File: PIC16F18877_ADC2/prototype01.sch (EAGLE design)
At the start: 16 parts, among them CN1 PIC_CN_H, CN2 ADC_IN, SW1 10-XX, U1 PIC16F18877-I/P, U2 AE-AQM1602A

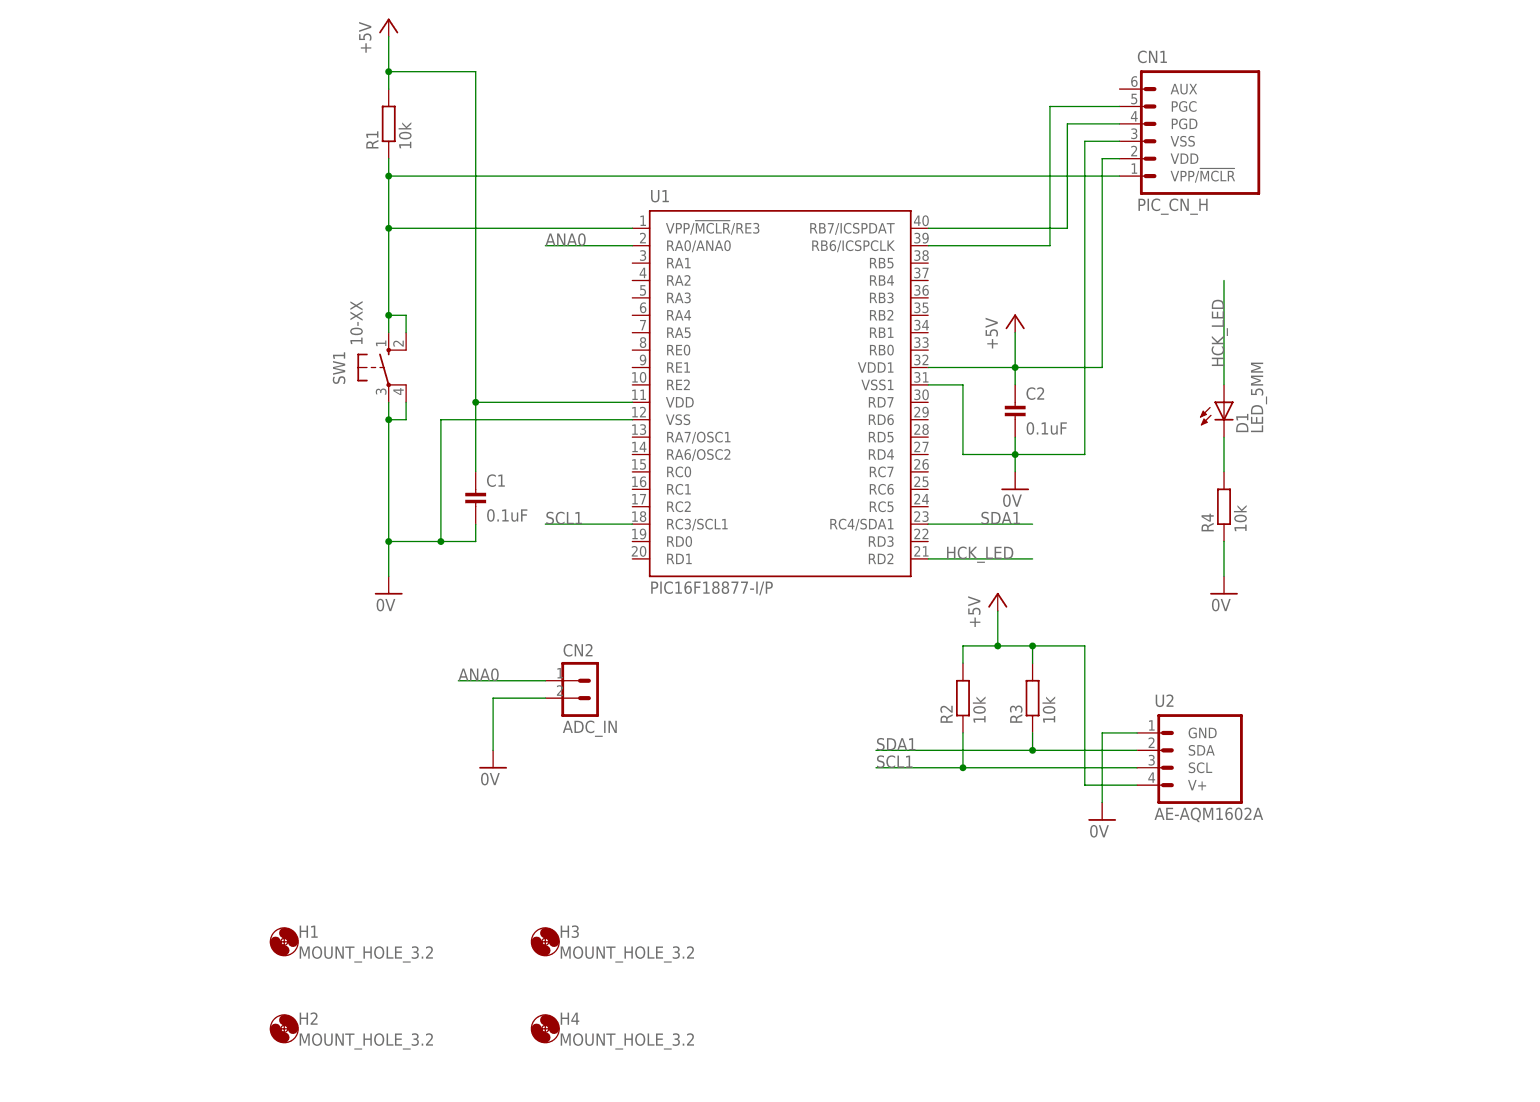
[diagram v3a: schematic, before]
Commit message: microSDカード接続のための回路図／コードを追加
sdcard、sdcard_testは、動作確認用の一時的なファイルなので後日必ず削除してください。
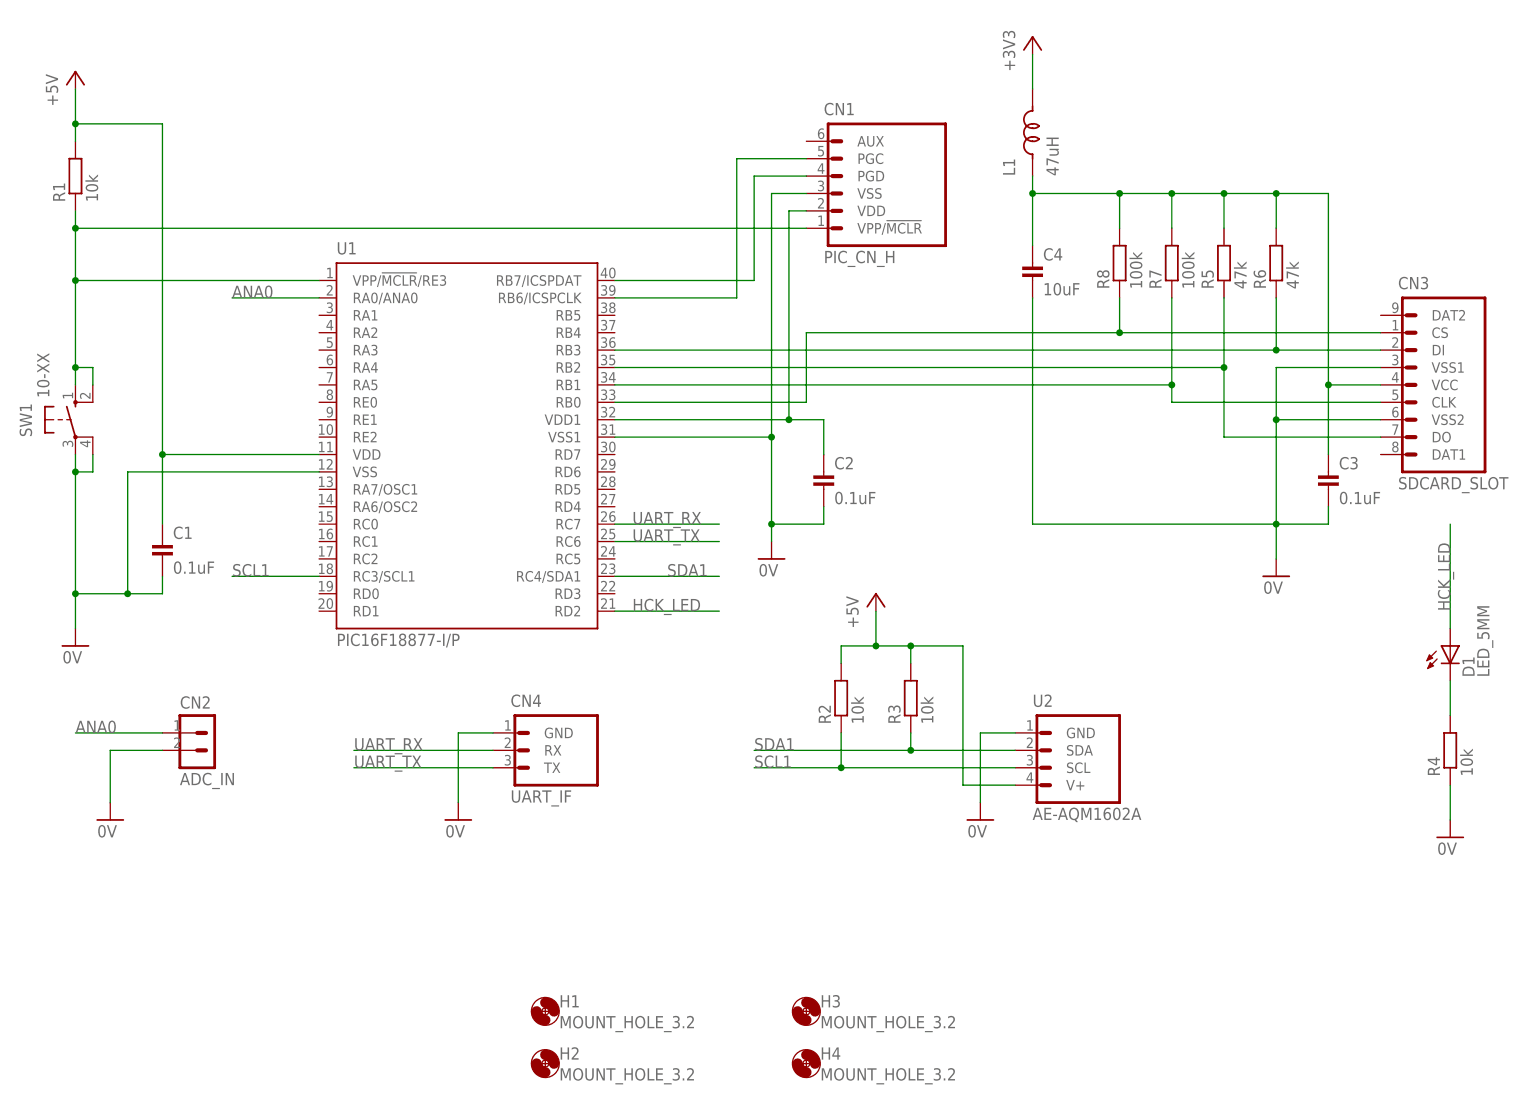
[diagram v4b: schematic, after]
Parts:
- added C3: 0.1uF, Parts:CAP_200MIL
- added C4: 10uF, Parts:CAP_200MIL
- added CN3: SDCARD_SLOT, PartsForProto:SDCARD_SLOT
- added CN4: UART_IF, PartsForProto:UART_IF
- added L1: 47uH, Parts:TC5026-22UH-060
- added R5, R6: 47k, Parts:RESISTOR_300MIL
- added R7, R8: 100k, Parts:RESISTOR_300MIL
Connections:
- new net +3V3: L1.2
- new net N$10: C2.1, CN1.VDD, U1.VDD1
- new net N$12: CN3.DI, R6.1, U1.RB3
- new net N$6: CN3.CLK, R7.1, U1.RB1
- new net N$7: CN3.CS, R8.1, U1.RB0
- new net N$8: CN3.DO, R5.1, U1.RB2
- new net N$9: C3.1, C4.1, CN3.VCC, L1.1, R5.2, R6.2, R7.2, R8.2
- new net UART_RX: CN4.RX, U1.RC7
- new net UART_TX: CN4.TX, U1.RC6
- net +5V: no longer C2.1, CN1.VDD, U1.VDD1
- net 0V: now also C3.2, C4.2, CN3.VSS1, CN3.VSS2, CN4.GND
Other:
- moved on the sheet: C1, C2, CN1, CN2, D1, H1, H2, H3, H4, R1, R2, R3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

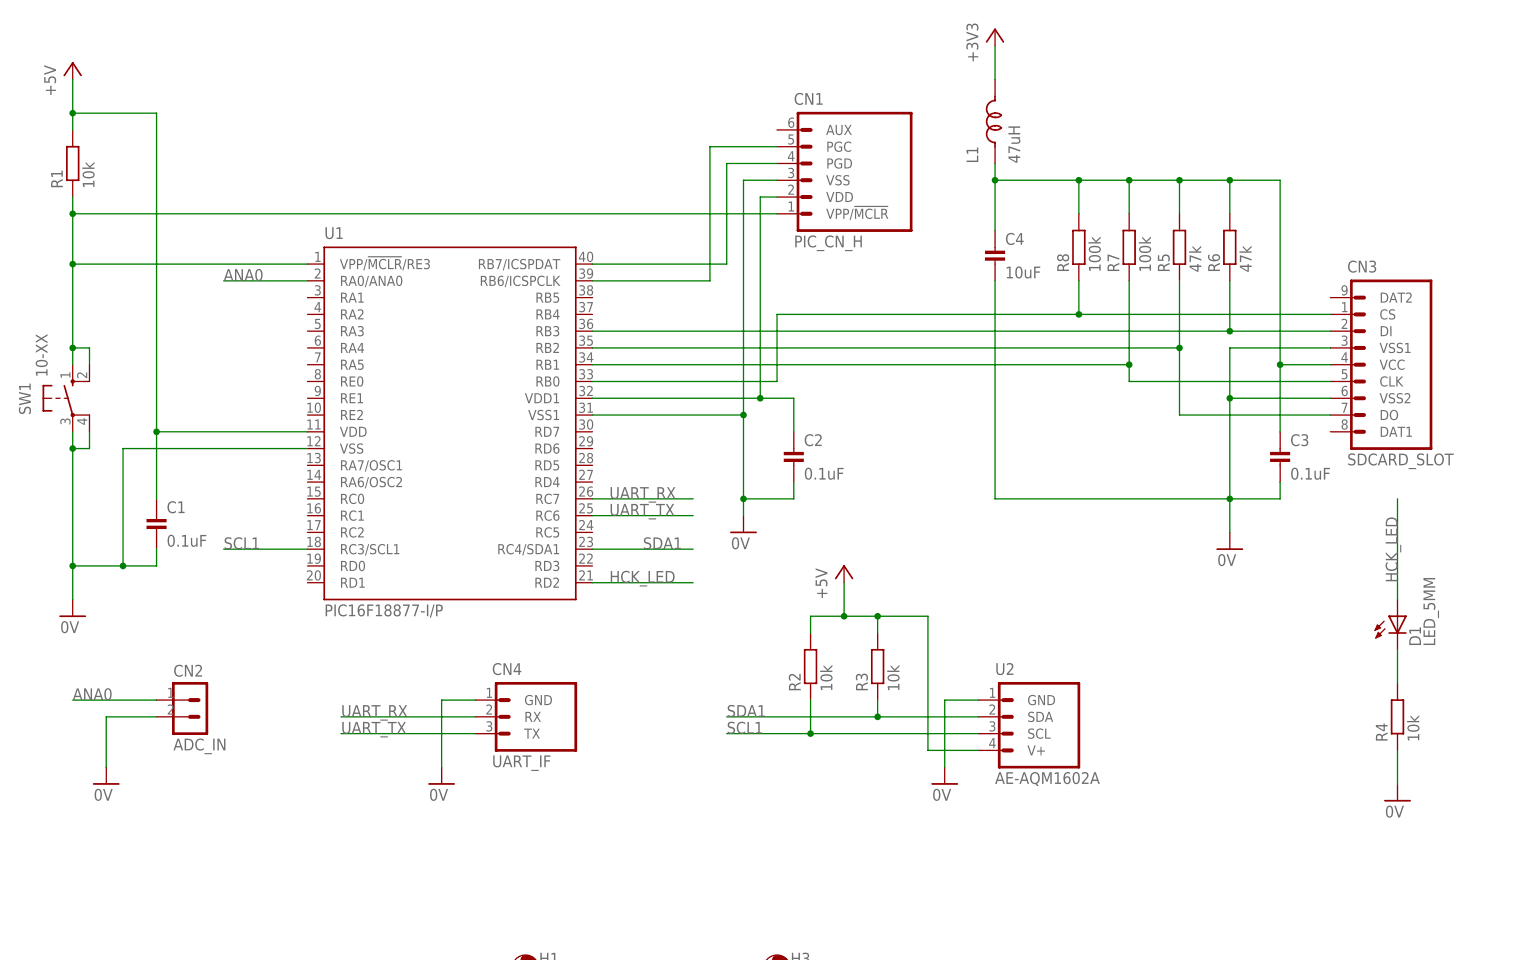
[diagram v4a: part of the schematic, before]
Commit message: 回路図を修正
マイクロＳＤカードスロットＤＩＰ化キットの使用を前提とするよう修正
http://akizukidenshi.com/catalog/g/gK-05488/
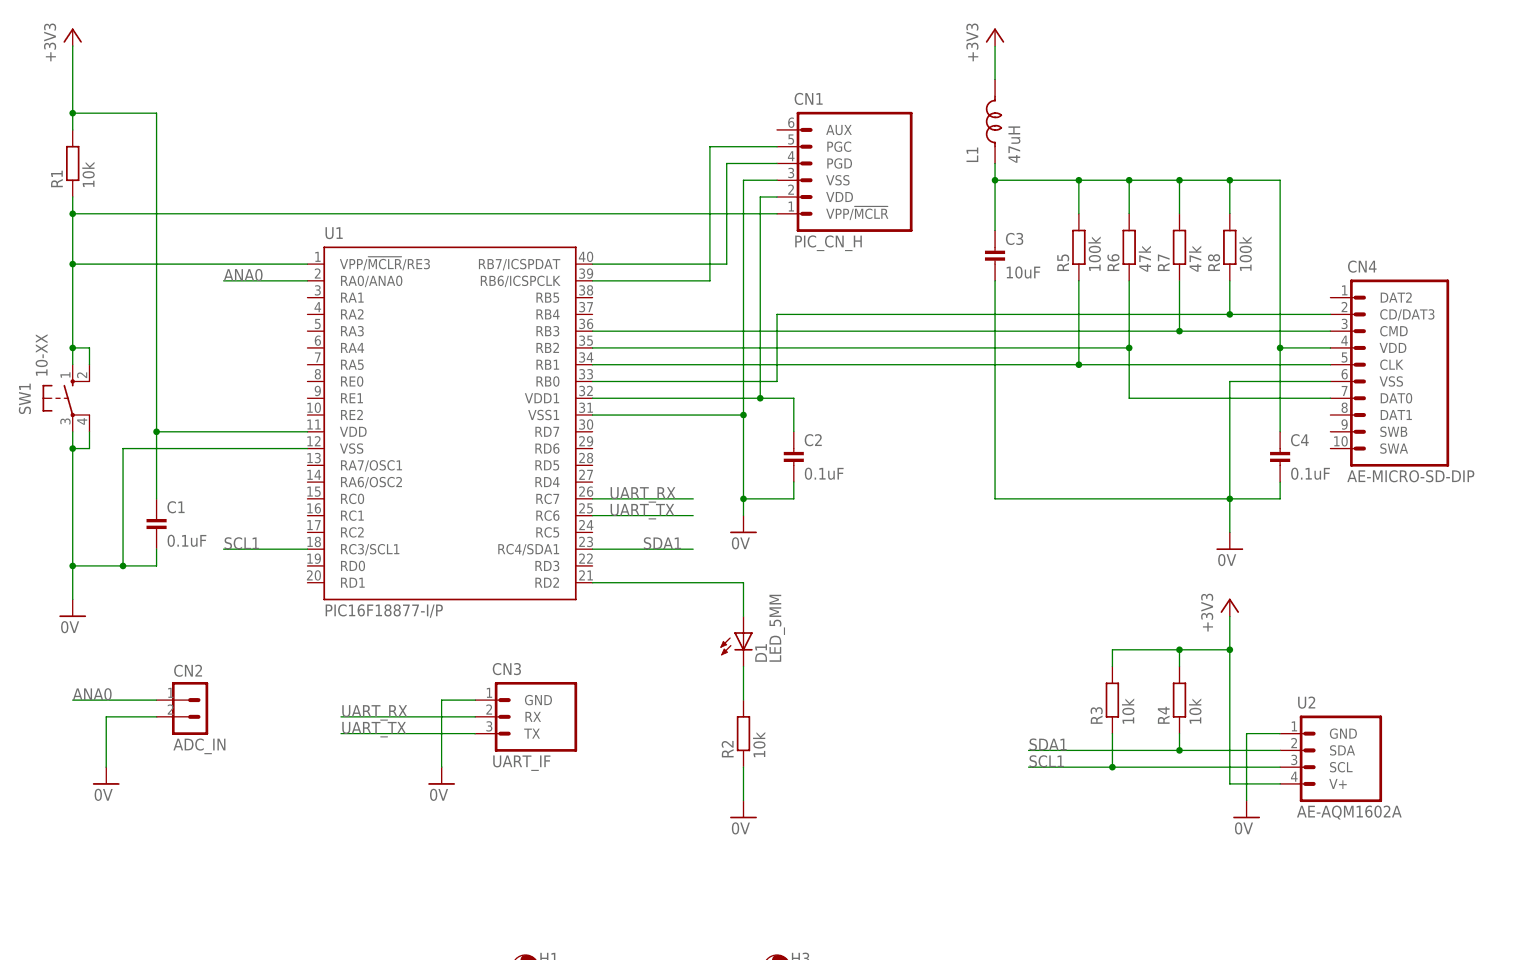
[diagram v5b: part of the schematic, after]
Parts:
- C3: value 0.1uF -> 10uF
- C4: value 10uF -> 0.1uF
- CN3: value SDCARD_SLOT -> UART_IF; device PartsForProto:SDCARD_SLOT -> PartsForProto:UART_IF
- CN4: value UART_IF -> AE-MICRO-SD-DIP; device PartsForProto:UART_IF -> PartsForProto:AE-MICRO-SD-DIP
- R5: value 47k -> 100k
- R7: value 100k -> 47k
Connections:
- net HCK_LED renamed N$5
- removed net +5V: C1.1, R1.2, R2.2, R3.2, U1.VDD, U2.V+
- net +3V3: now also C1.1, R1.2, R3.2, R4.2, U1.VDD, U2.V+
- net 0V: now also CN3.GND, CN4.VSS, R2.1; no longer CN3.VSS1, CN3.VSS2, CN4.GND, R4.1
- net N$1: now also R2.2; no longer R4.2
- net N$12: now also CN4.CMD, R7.1; no longer CN3.DI, R6.1
- net N$6: now also CN4.CLK, R5.1; no longer CN3.CLK, R7.1
- net N$7: now also CN4.CD/DAT3; no longer CN3.CS
- net N$8: now also CN4.DAT0, R6.1; no longer CN3.DO, R5.1
- net N$9: now also CN4.VDD; no longer CN3.VCC
- net SCL1: now also R3.1; no longer R2.1
- net SDA1: now also R4.1; no longer R3.1
- net UART_RX: now also CN3.RX; no longer CN4.RX
- net UART_TX: now also CN3.TX; no longer CN4.TX
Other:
- moved on the sheet: C3, C4, D1, R2, R3, R4, R5, R6, R7, R8, U2
